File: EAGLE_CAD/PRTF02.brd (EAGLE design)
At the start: 70 x 70 mm, 73 parts

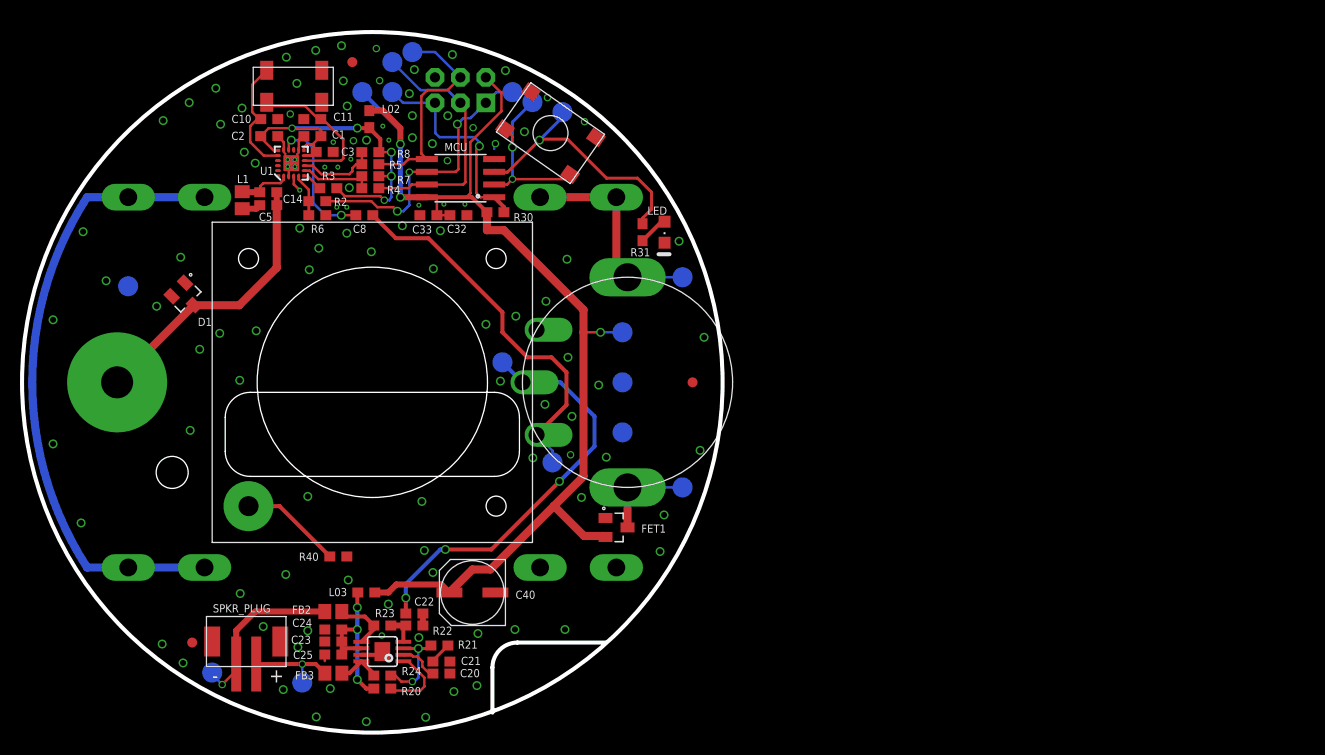
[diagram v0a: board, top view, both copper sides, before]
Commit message: Very very small changes to layout
Deleted a few vias that seemed problematic.
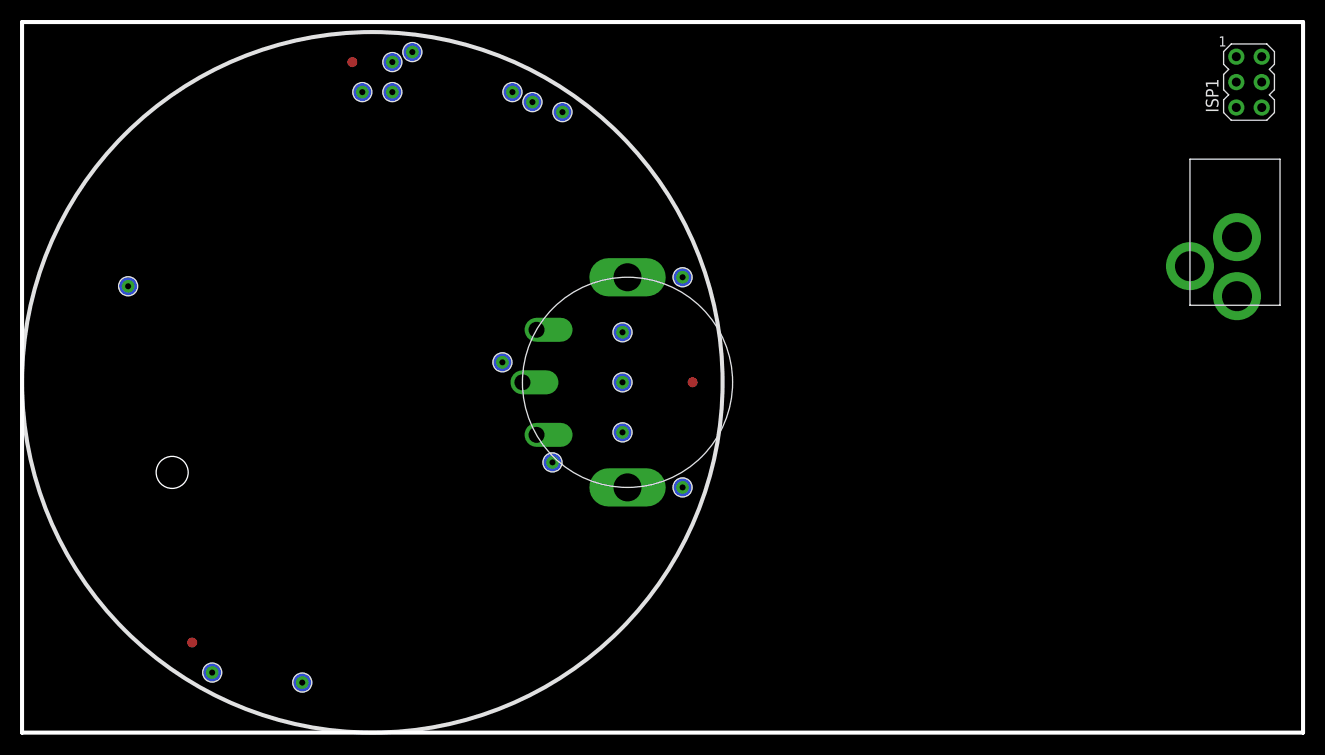
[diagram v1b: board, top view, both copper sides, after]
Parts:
- removed AMP: (no value), PR_Parts_Library:8-MSOP
- removed ANT_MOUNT: DNP, PR_Parts_Library:M3_BOLT_HOLE
- removed C1, C2: 22nF, PR_Parts_Library:0603_CPL
- removed C10, C11: 22pF, PR_Parts_Library:0603_CPL
- removed C14: 47pF, PR_Parts_Library:0603_CPL
- removed C20, C21, C22: .22uF, PR_Parts_Library:0603_CPL
- removed C23, C3, C33: .1uF, PR_Parts_Library:0603_CPL
- removed C24, C8: 1uF, PR_Parts_Library:0603_CPL
- removed C25, C32: 10uF, PR_Parts_Library:0603_CPL
- removed C40: 220uF, PR_Parts_Library:NICHICON_UD_63
- removed C5, R40: DNP, PR_Parts_Library:0603_CPL
- removed D1, FET1: (no value), PR_Parts_Library:SOT23_CPL
- removed FB2, FB3: (no value), PR_Parts_Library:0805_ADAFRUIT
- removed ISP: (no value), PR_Parts_Library:2X3-NS
- removed JP5, JP6: (no value), PR_Parts_Library:BK92_AA_BATT
- removed L02, L03: 2.2k@100MHz, PR_Parts_Library:0603_CPL
- removed L1: 180nH, PR_Parts_Library:0805_ADAFRUIT
- removed LED: (no value), adafruit:CHIPLED_0805
- removed MCU: (no value), PR_Parts_Library:8-SOIC
- removed R2, R4, R5: 330, PR_Parts_Library:0603_CPL
- removed R20, R30, R6: 10K, PR_Parts_Library:0603_CPL
- removed R21, R22: 12K, PR_Parts_Library:0603_CPL
- removed R23, R24: 100K, PR_Parts_Library:0603_CPL
- removed R3, R7, R8: 4.7K, PR_Parts_Library:0603_CPL
- removed R31: 1K, PR_Parts_Library:0603_CPL
- removed SPKR_PLACE: DNP, PR_Parts_Library:PR2023_SPKR_PLACE
- removed SPKR_PLUG: (no value), PR_Parts_Library:JST-B2B-PH-SM4-TB
- removed SW1: (no value), PR_Parts_Library:C&K_PTS645_SMT
- removed U1: (no value), PR_Parts_Library:SI470X_20_QFN
- removed X1: (no value), PR_Parts_Library:4-SOJ
- added ISP1: AVRISP-6, adafruit:AVRISP
- added U$10, U$11, U$12, U$13, U$14, U$15, U$16, U$17, U$18, U$2, U$3, U$4, U$5, U$6, U$7, U$8, U$9: 0908MILL_MAX_SPRINGPIN, PR_Parts_Library:0908MILL_MAX_SPRINGPIN
- added U$19: 2.1MMJACKTHM, adafruit:PJ-102A
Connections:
- removed net !RST-L: R2.2, R6.2, U1.5
- removed net !SEN-L: R3.1, U1.6
- removed net 3.3V: C1.1, C2.1, C3.1, L02.2, R3.2, R7.2, R8.2, U1.10, U1.11, U1.16
- removed net ANT: ANT_MOUNT.P$1, C14.1, C5.1, D1.3
- removed net GPIO1: U1.19
- removed net GPIO2: U1.18
- removed net N$1: C11.1, U1.9, X1.P$1
- removed net N$10: C10.1, U1.17, X1.P$4
- removed net N$11: AMP.8, FB3.2, R24.1
- removed net N$12: AMP.2, C20.2
- removed net N$13: JP5.NEG, JP5.NEG@2, JP6.POS, JP6.POS@2
- removed net N$14: AMP.4, R22.1, R23.1
- removed net N$16: C14.2, L1.1, U1.2
- removed net N$2: AMP.6, C23.1, C24.1, C25.1, L03.2, R20.2
- removed net N$20: AMP.1, R20.1
- removed net N$23: C21.2, R21.1
- removed net N$3: C22.1, R22.2
- removed net N$4: AMP.5, FB2.1, R23.2
- removed net N$5: AMP.3, R21.2, R24.2
- removed net N$7: LED.A, R31.1
- removed net N$8: R40.2, SPKR_PLACE.LID_GND
- removed net N$9: C8.1, U1.14
- removed net SCLK-L: R4.2, R7.1, U1.7
- removed net SDIO-L: R5.2, R8.1, U1.8
- new net MISO: ISP1.1, U$11.P$1
- new net MOSI: ISP1.4, U$14.P$1
- new net RST: ISP1.5
- new net SCK: ISP1.3, U$12.P$1
- net !RST: no longer ISP.1, MCU.6, R2.1
- net A_IN: now also U$17.P$1; no longer C8.2
- net A_OUT: now also U$18.P$1; no longer C22.2
- net GND: now also ISP1.6, U$2.P$1, U$3.P$1, U$4.P$1; no longer AMP.7, AMP.9, C1.2, C10.2, C11.2, C2.2, C20.1, C21.1, C23.2, C24.2, C25.2, C3.2, C32.2, C33.2, C40.P$2, C5.2, D1.1, D1.2, FET1.1, ISP.6, JP6.NEG, JP6.NEG@2, L1.2, LED.C, MCU.4, R40.1, R6.1, SW1.P$1, SW1.P$2, U1.12, U1.15, U1.21, U1.3, U1.4
- net LED/PB4: now also U$10.P$1; no longer MCU.3, R31.2
- net RESET: now also U$13.P$1; no longer ISP.5, MCU.1, R30.2
- net SCLK: no longer ISP.3, MCU.7, R4.1
- net SDIO: no longer ISP.4, MCU.5, R5.1
- net SPK_OUT+: now also U$7.P$1; no longer FB2.2, SPKR_PLUG.2
- net SPK_OUT-: now also U$8.P$1; no longer FB3.1, SPKR_PLUG.1
- net SW: now also U$9.P$1; no longer MCU.2, SW1.P$3, SW1.P$4
- net SW_IN: now also U$15.P$1; no longer FET1.3
- net SW_OUT: now also U$16.P$1; no longer JP5.POS, JP5.POS@2
- net VCC: now also ISP1.2, U$5.P$1, U$6.P$1; no longer C32.1, C33.1, C40.P$1, FET1.2, ISP.2, L02.1, L03.1, MCU.8, R30.1
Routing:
- net VCC: track 115.0 -> 0.00 mm, vias 3 -> 0
- net N$13: track 60.5 -> 0.00 mm
- net A_OUT: track 42.1 -> 0.00 mm, vias 3 -> 0
- net 3.3V: track 39.7 -> 0.00 mm, vias 5 -> 0
- net A_IN: track 37.9 -> 0.00 mm
- net !RST: track 28.8 -> 0.00 mm, vias 3 -> 0
- net ANT: track 28.3 -> 0.00 mm
- net LED/PB4: track 26.8 -> 0.00 mm, vias 1 -> 0
- net SCLK: track 25.6 -> 0.00 mm
- net SDIO: track 22.1 -> 0.00 mm
- net RESET: track 21.6 -> 0.00 mm, vias 1 -> 0
- net SW_OUT: track 21.6 -> 0.00 mm
- net SW: track 18.7 -> 0.00 mm, vias 2 -> 0
- net SPK_OUT+: track 17.2 -> 0.00 mm, vias 1 -> 0
- net N$2: track 16.7 -> 0.00 mm, vias 3 -> 0
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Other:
- board size 70 x 70 mm -> 128 x 71 mm
